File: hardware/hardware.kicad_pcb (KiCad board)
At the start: 2 copper layers, 61.3 x 54.1 mm, 28 parts, among them J1 Conn_01x10_Socket, J2 Conn_01x10_Socket, J3 Conn_01x10_Socket, J4 Conn_01x10_Socket, J5 Conn_01x10_Pin, J6 Conn_01x10_Pin, J7 Conn_01x10_Pin, J8 Conn_01x10_Pin

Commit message: fix pcb planes
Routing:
- net +5V: track 260.7 -> 257.7 mm, vias 10 -> 12
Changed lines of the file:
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@@
+	)
+	(segment
+		(start 90.551 120.523)
+		(end 92.164 122.136)
+		(width 0.2)
+		(layer "F.Cu")
+		(net 56)
 	)
 	(segment
@@
 	)
 	(segment
+		(start 92.164 122.136)
+		(end 92.167 122.136)
+		(width 0.2)
+		(layer "F.Cu")
+		(net 56)
+	)
+	(segment
 		(start 70.483 115.443)
 		(end 70.483 115.191)
@@
 	)
 	(via
+		(at 90.551 120.523)
+		(size 0.6)
+		(drill 0.3)
+		(layers "F.Cu" "B.Cu")
+		(net 56)
+	)
+	(via
 		(at 71.12 83.82)
 		(size 0.6)
@@
 	(via
 		(at 71.12 74.168)
+		(size 0.6)
+		(drill 0.3)
+		(layers "F.Cu" "B.Cu")
+		(net 56)
+	)
+	(via
+		(at 92.167 122.136)
 		(size 0.6)
 		(drill 0.3)
@@
 	)
 	(segment
-		(start 90.551 120.523)
-		(end 90.551 100.076)
-		(width 0.2)
-		(layer "B.Cu")
-		(net 56)
-	)
-	(segment
-		(start 109.566 69.434)
-		(end 109.093 69.434)
-		(width 0.2)
-		(layer "B.Cu")
-		(net 56)
-	)
-	(segment
 		(start 78.1304 97.3836)
 		(end 82.042 97.3836)
@@
 	)
 	(segment
-		(start 109.093 69.434)
-		(end 96.428 69.434)
-		(width 0.2)
-		(layer "B.Cu")
-		(net 56)
-	)
-	(segment
-		(start 96.428 69.434)
-		(end 90.932 74.93)
+		(start 116.459 76.327)
+		(end 113.1697 73.0377)
 		(width 0.2)
 		(layer "B.Cu")
@@
 	)
 	(segment
+		(start 90.551 120.523)
+		(end 90.551 120.4214)
+		(width 0.2)
+		(layer "B.Cu")
+		(net 56)
+	)
+	(segment
 		(start 71.12 94.488)
 		(end 71.882 94.488)
@@
 	)
 	(segment
+		(start 90.932 74.93)
+		(end 92.8992 72.9628)
+		(width 0.2)
+		(layer "B.Cu")
+		(net 56)
+	)
+	(segment
 		(start 71.12 83.82)
 		(end 71.882 83.82)
@@
 	)
 	(segment
+		(start 113.0948 72.9628)
+		(end 113.1697 73.0377)
+		(width 0.2)
+		(layer "B.Cu")
+		(net 56)
+	)
+	(segment
 		(start 81.6864 97.3836)
 		(end 80.2132 95.9104)
@@
 	)
 	(segment
-		(start 116.459 76.327)
-		(end 109.566 69.434)
-		(width 0.2)
-		(layer "B.Cu")
-		(net 56)
-	)
-	(segment
 		(start 80.2132 92.964)
 		(end 80.2132 95.9104)
@@
 	)
 	(segment
+		(start 90.551 120.4214)
+		(end 90.551 100.076)
+		(width 0.2)
+		(layer "B.Cu")
+		(net 56)
+	)
+	(segment
 		(start 116.000744 84.596744)
 		(end 116.000744 76.785256)
@@
 	)
 	(segment
-		(start 92.167 122.139)
-		(end 90.551 120.523)
-		(width 0.2)
-		(layer "B.Cu")
+		(start 92.8992 72.9628)
+		(end 113.0948 72.9628)
+		(width 0.2)
+		(layer "B.Cu")

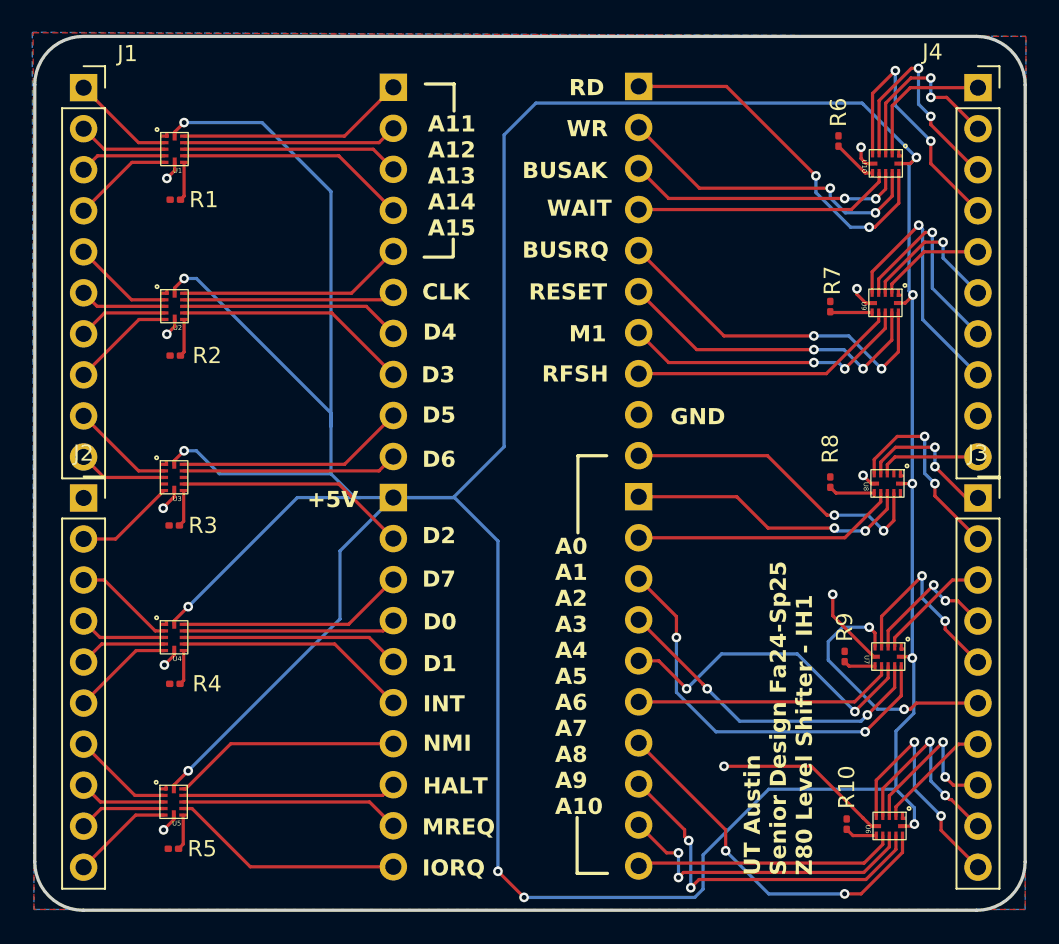
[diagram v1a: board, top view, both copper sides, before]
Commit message: add XC7S15 8x8 BGA footprint and symbol to kicad project
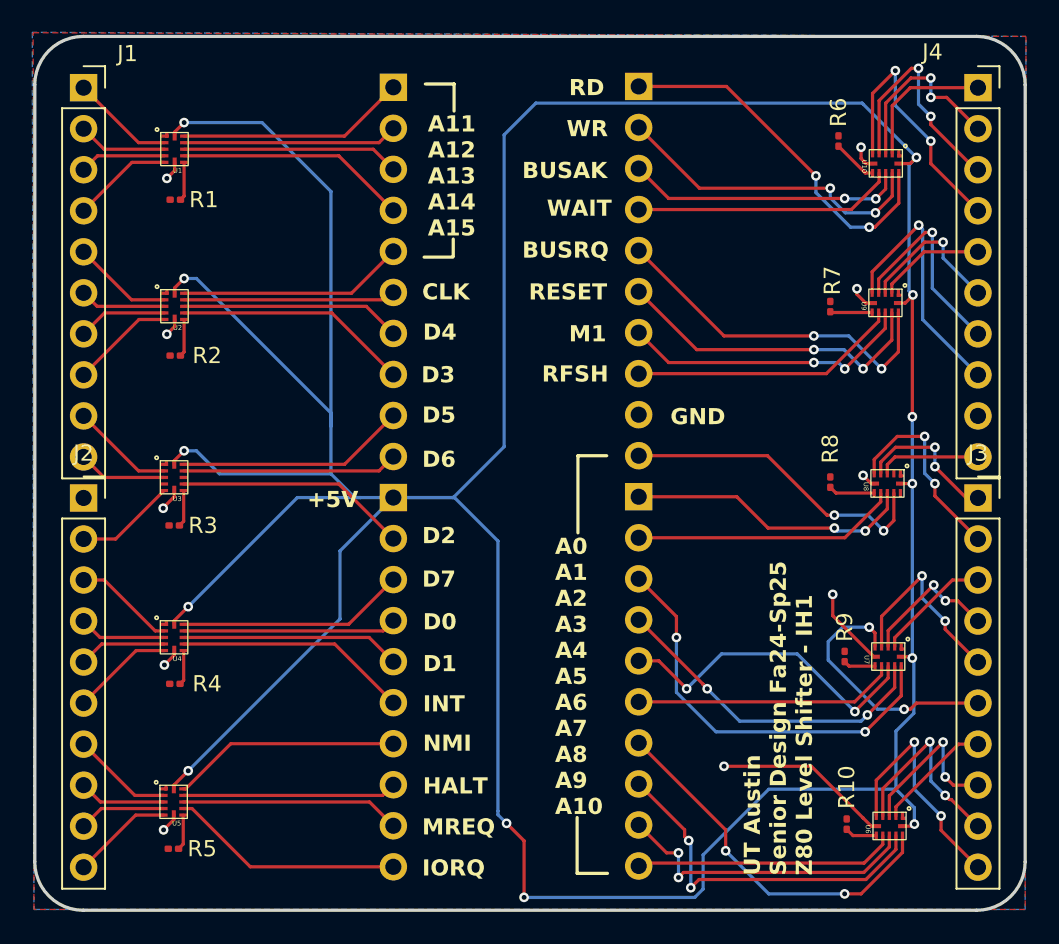
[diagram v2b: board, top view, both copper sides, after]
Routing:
- net +5V: track 257.7 -> 257.8 mm, vias 12 -> 13
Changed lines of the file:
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@@
+	)
+	(segment
+		(start 116.205 84.871)
+		(end 116.24 84.836)
+		(width 0.2)
+		(layer "F.Cu")
+		(net 56)
 	)
 	(segment
@@
 	)
 	(segment
+		(start 91.0844 117.5512)
+		(end 92.167 118.6338)
+		(width 0.2)
+		(layer "F.Cu")
+		(net 56)
+	)
+	(segment
+		(start 116.205 92.3798)
+		(end 116.205 84.871)
+		(width 0.2)
+		(layer "F.Cu")
+		(net 56)
+	)
+	(segment
 		(start 70.5358 75.0316)
 		(end 70.5358 74.7522)
@@
 	)
 	(segment
+		(start 92.167 118.6338)
+		(end 92.167 122.136)
+		(width 0.2)
+		(layer "F.Cu")
+		(net 56)
+	)
+	(segment
 		(start 116.1288 107.2388)
 		(end 116.205 107.315)
@@
 	)
 	(segment
-		(start 90.551 120.523)
-		(end 92.164 122.136)
-		(width 0.2)
-		(layer "F.Cu")
-		(net 56)
-	)
-	(segment
 		(start 115.3414 76.7072)
 		(end 116.0788 76.7072)
@@
 	)
 	(via
+		(at 91.0844 117.5512)
+		(size 0.6)
+		(drill 0.3)
+		(layers "F.Cu" "B.Cu")
+		(net 56)
+	)
+	(via
 		(at 116.205 96.52)
 		(size 0.6)
@@
 	)
 	(via
-		(at 90.551 120.523)
-		(size 0.6)
-		(drill 0.3)
-		(layers "F.Cu" "B.Cu")
-		(net 56)
-	)
-	(via
 		(at 71.12 83.82)
+		(size 0.6)
+		(drill 0.3)
+		(layers "F.Cu" "B.Cu")
+		(net 56)
+	)
+	(via
+		(at 116.205 92.3798)
 		(size 0.6)
 		(drill 0.3)
@@
 	)
 	(segment
-		(start 116.205 96.52)
-		(end 116.205 84.871)
-		(width 0.2)
-		(layer "B.Cu")
-		(net 56)
-	)
-	(segment
 		(start 71.374 104.14)
 		(end 78.1304 97.3836)
@@
 	)
 	(segment
-		(start 90.551 120.523)
-		(end 90.551 120.4214)
-		(width 0.2)
-		(layer "B.Cu")
-		(net 56)
-	)
-	(segment
 		(start 71.12 94.488)
 		(end 71.882 94.488)
@@
 	)
 	(segment
+		(start 116.205 96.52)
+		(end 116.205 92.3798)
+		(width 0.2)
+		(layer "B.Cu")
+		(net 56)
+	)
+	(segment
 		(start 73.3044 95.9104)
 		(end 80.2132 95.9104)
@@
 	)
 	(segment
-		(start 90.551 120.4214)
-		(end 90.551 100.076)
-		(width 0.2)
-		(layer "B.Cu")
-		(net 56)
-	)
-	(segment
 		(start 116.000744 84.596744)
 		(end 116.000744 76.785256)
@@
 	)
 	(segment
+		(start 90.551 117.0178)
+		(end 91.0844 117.5512)
+		(width 0.2)
+		(layer "B.Cu")
+		(net 56)
+	)
+	(segment
 		(start 116.24 84.836)
 		(end 116.000744 84.596744)
@@
 	)
 	(segment
+		(start 90.551 116.7892)
+		(end 90.551 100.076)
+		(width 0.2)
+		(layer "B.Cu")
+		(net 56)
+	)
+	(segment
 		(start 80.2132 92.1512)
 		(end 80.2132 92.964)
@@
 		(width 0.2)
 		(layer "B.Cu")
+		(net 56)
+	)
+	(segment
+		(start 90.551 116.7892)
+		(end 90.551 117.0178)
+		(width 0.2)
+		(layer "B.Cu")
